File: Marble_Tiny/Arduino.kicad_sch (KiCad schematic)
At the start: 17 parts

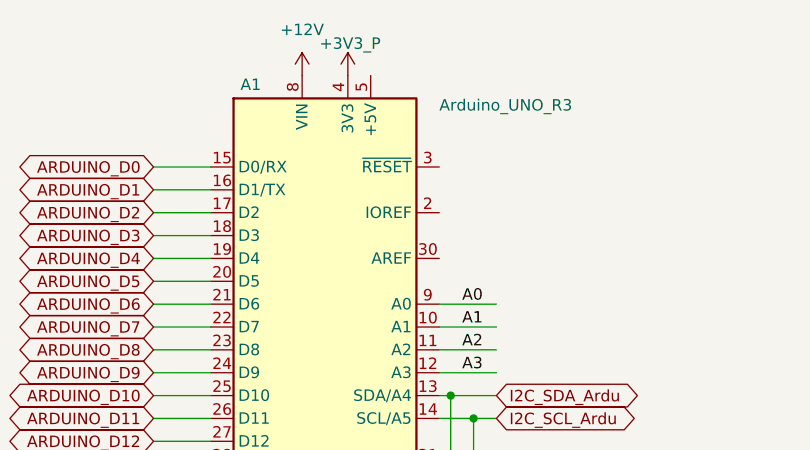
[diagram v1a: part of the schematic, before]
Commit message: fixed ERCs; added test points; added WP switch
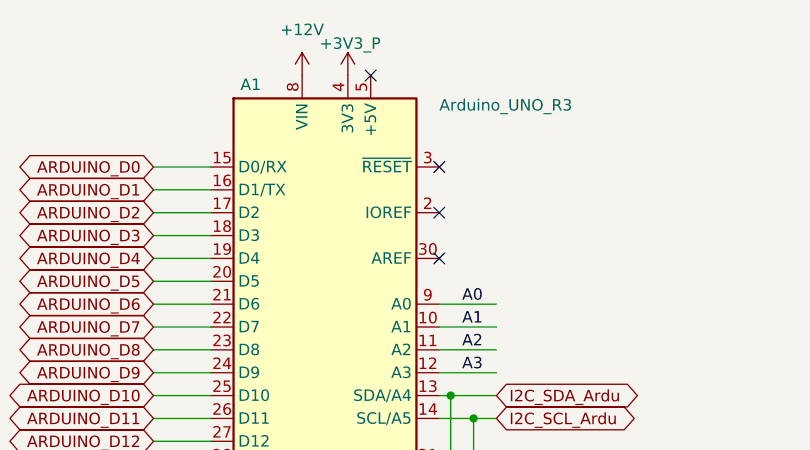
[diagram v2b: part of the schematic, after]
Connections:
- no-connect marks 0 -> 4
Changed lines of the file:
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@@
 		(color 0 0 0 0)
+	)
+	(no_connect
+		(at 151.13 69.85)
+	)
+	(no_connect
+		(at 151.13 74.93)
+	)
+	(no_connect
+		(at 151.13 80.01)
+	)
+	(no_connect
+		(at 143.51 59.69)
 	)
 	(wire

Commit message: fixed issue with PMODs; added board name and revision; fixed polygons issue
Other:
- company: (none) -> ${name}
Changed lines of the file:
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@@
 	(generator_version "9.0")
 	(paper "A4")
+	(title_block
+		(date "2025-04-18")
+		(rev "${rev}")
+		(company "${name}")
+		(comment 1 "${author}")
+	)
 	(junction
 		(at 154.94 97.79)
